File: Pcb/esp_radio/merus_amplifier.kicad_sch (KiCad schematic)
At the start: 2 parts, among them J5 MERUS I2S, J6 MERUS I2C

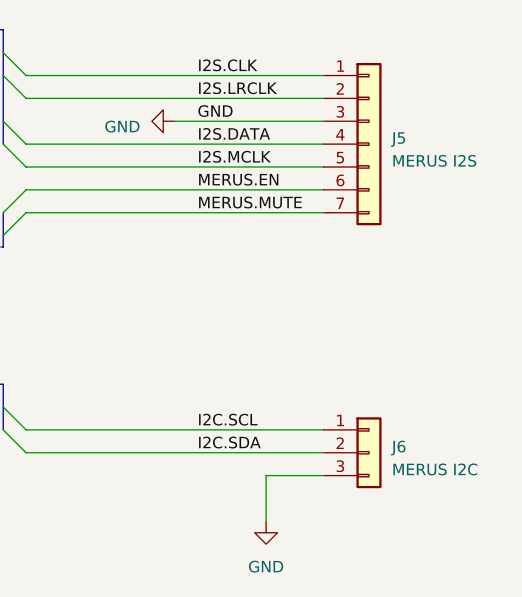
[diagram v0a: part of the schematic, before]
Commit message: Move custom components to kicad_common_library.
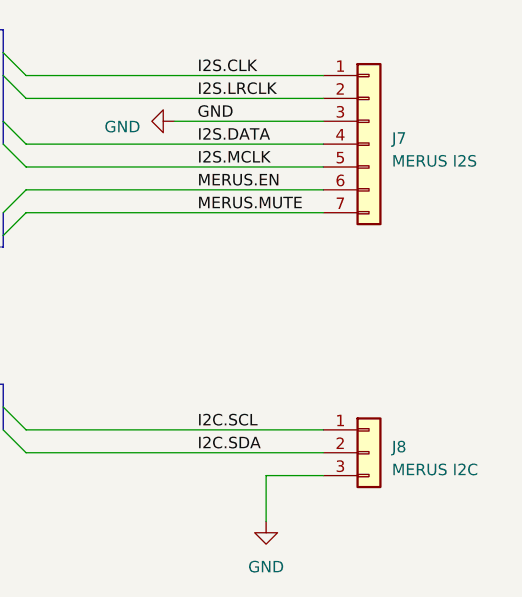
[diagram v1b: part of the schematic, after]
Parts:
- renumbered J5 to J7, J6 to J8
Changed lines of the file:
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@@
   (symbol (lib_id "Connector_Generic:Conn_01x07") (at 170.18 80.01 0) (unit 1)
     (in_bom yes) (on_board yes) (dnp no) (fields_autoplaced)
-    (property "Reference" "J5" (at 172.72 79.375 0)
+    (property "Reference" "J7" (at 172.72 79.375 0)
       (effects (font (size 1.27 1.27)) (justify left))
     )
@@
       (project "esp_radio"
         (path "/c9e2e0d2-0655-4f5e-8e13-71b41b1f7cfe/0a87a903-62c1-40b5-b380-98c846d36513"
-          (reference "J5") (unit 1)
+          (reference "J7") (unit 1)
         )
       )
@@
   (symbol (lib_id "power:GND") (at 158.75 121.92 0) (unit 1)
     (in_bom yes) (on_board yes) (dnp no) (fields_autoplaced)
-    (property "Reference" "#PWR047" (at 158.75 128.27 0)
+    (property "Reference" "#PWR058" (at 158.75 128.27 0)
       (effects (font (size 1.27 1.27)) hide)
     )
@@
       (project "esp_radio"
         (path "/c9e2e0d2-0655-4f5e-8e13-71b41b1f7cfe/0a87a903-62c1-40b5-b380-98c846d36513"
-          (reference "#PWR047") (unit 1)
+          (reference "#PWR058") (unit 1)
         )
       )
@@
   (symbol (lib_id "power:GND") (at 148.59 77.47 270) (unit 1)
     (in_bom yes) (on_board yes) (dnp no) (fields_autoplaced)
-    (property "Reference" "#PWR046" (at 142.24 77.47 0)
+    (property "Reference" "#PWR057" (at 142.24 77.47 0)
       (effects (font (size 1.27 1.27)) hide)
     )
@@
       (project "esp_radio"
         (path "/c9e2e0d2-0655-4f5e-8e13-71b41b1f7cfe/0a87a903-62c1-40b5-b380-98c846d36513"
-          (reference "#PWR046") (unit 1)
+          (reference "#PWR057") (unit 1)
         )
       )
@@
   (symbol (lib_id "Connector_Generic:Conn_01x03") (at 170.18 114.3 0) (unit 1)
     (in_bom yes) (on_board yes) (dnp no) (fields_autoplaced)
-    (property "Reference" "J6" (at 172.72 113.665 0)
+    (property "Reference" "J8" (at 172.72 113.665 0)
       (effects (font (size 1.27 1.27)) (justify left))
     )
@@
       (project "esp_radio"
         (path "/c9e2e0d2-0655-4f5e-8e13-71b41b1f7cfe/0a87a903-62c1-40b5-b380-98c846d36513"
-          (reference "J6") (unit 1)
+          (reference "J8") (unit 1)
         )
       )

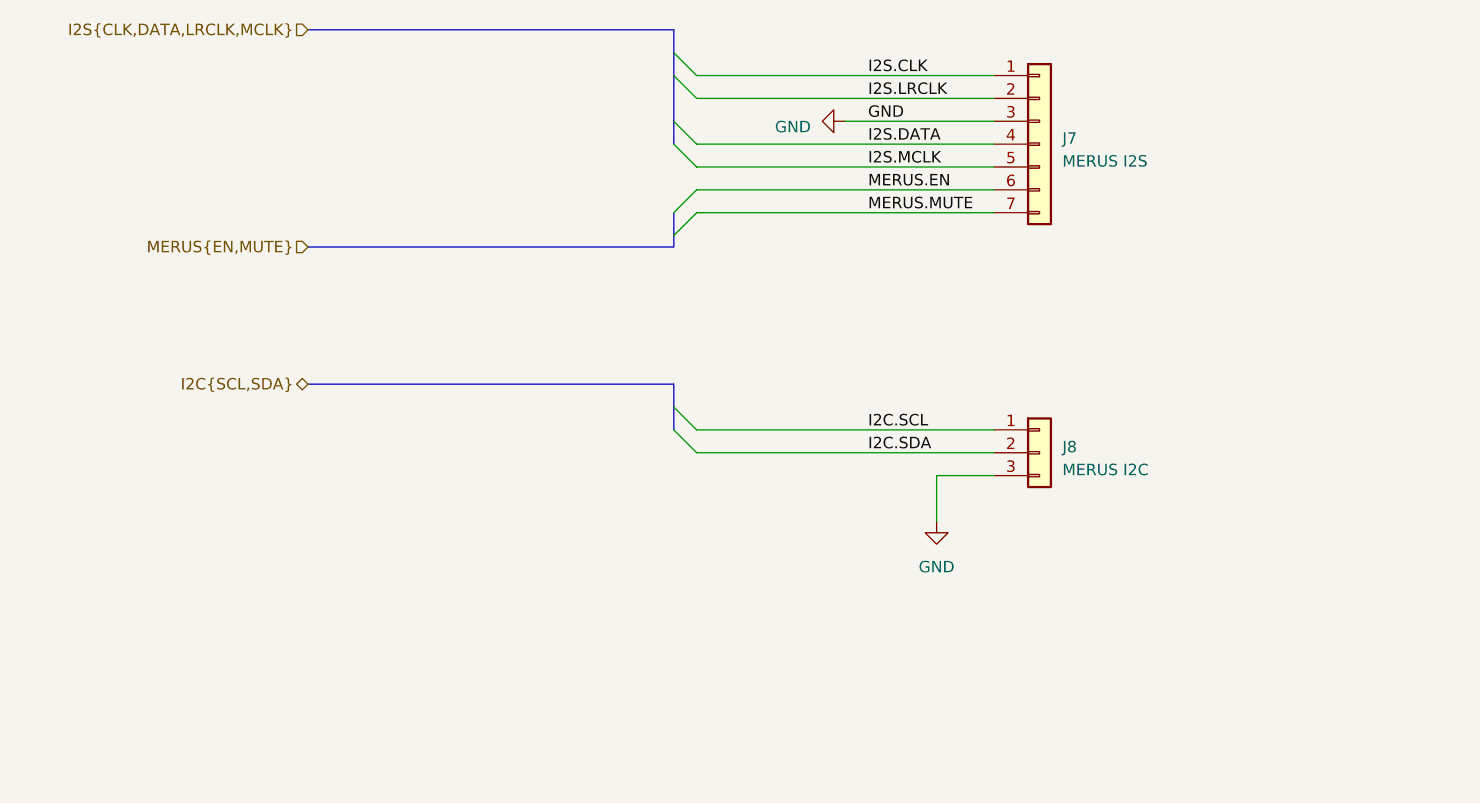
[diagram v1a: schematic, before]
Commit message: Add components layout on PCB
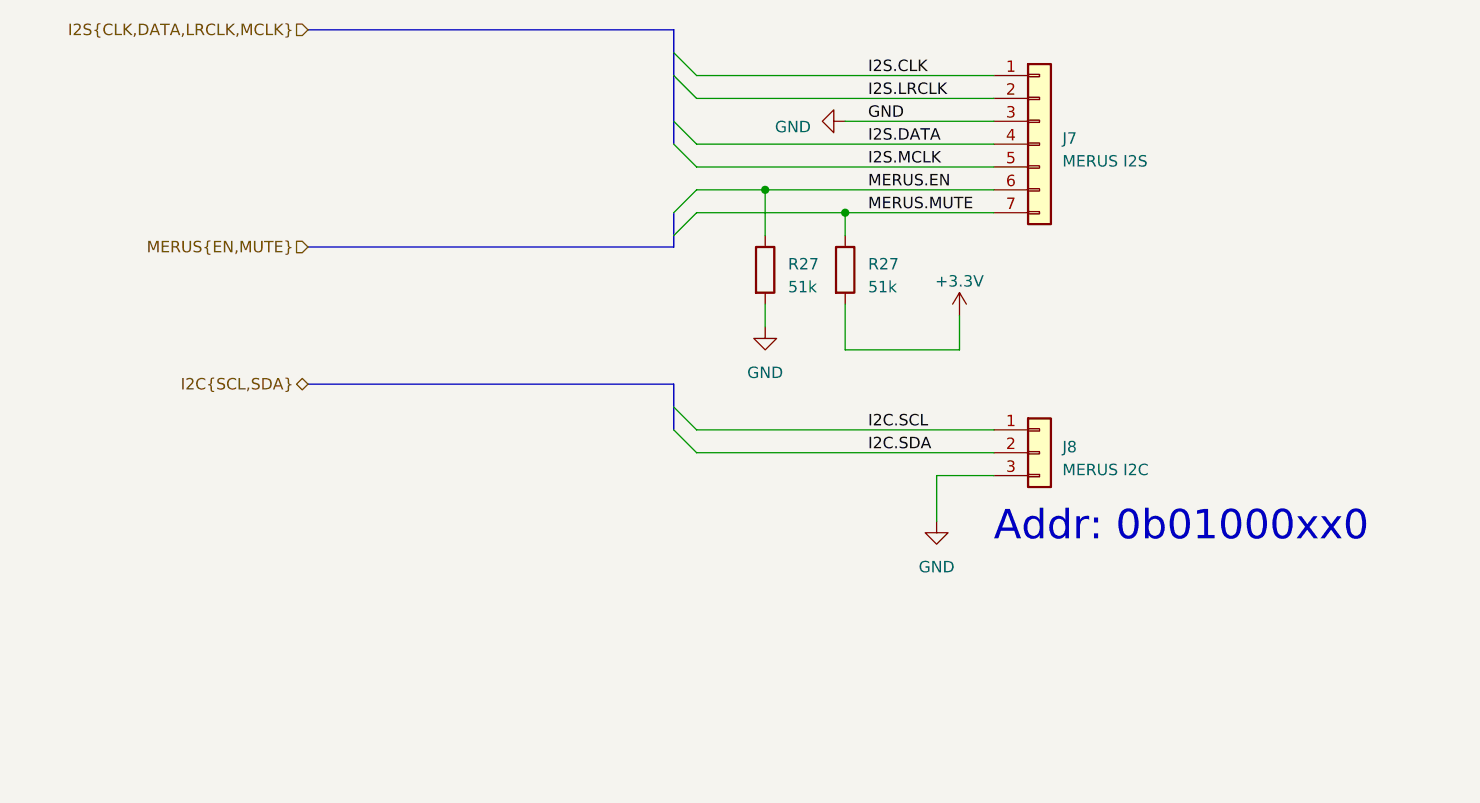
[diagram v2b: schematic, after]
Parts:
- added R27 (x2): 51k, kicad_common_lib:R_0805, symbol Device:R
- J7: footprint (none) -> Connector_JST:JST_XH_S7B-XH-A_1x07_P2.50mm_Horizontal
- J8: footprint (none) -> Connector_JST:JST_XH_S3B-XH-A_1x03_P2.50mm_Horizontal
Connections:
- net GND: now also R27.2
- net MERUS.EN: now also R27.1
- net MERUS.MUTE: now also R27.1
- new net +3.3V: R27.2
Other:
- note added: "Addr: 0b01000xx0"
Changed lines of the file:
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@@
 (kicad_sch (version 20230121) (generator eeschema)
   (paper "A4")
+  (junction (at 148.59 87.63) (diameter 0) (color 0 0 0 0)
+  )
+  (junction (at 139.7 85.09) (diameter 0) (color 0 0 0 0)
+  )
   (bus_entry (at 129.54 69.85) (size 2.54 2.54)
     (stroke (width 0) (type default))
@@
     (stroke (width 0) (type default))
   )
+  (wire (pts (xy 148.59 87.63) (xy 148.59 90.17))
+    (stroke (width 0) (type default))
+  )
   (bus (pts (xy 129.54 67.31) (xy 129.54 69.85))
     (stroke (width 0) (type default))
@@
     (stroke (width 0) (type default))
   )
+  (wire (pts (xy 148.59 102.87) (xy 161.29 102.87))
+    (stroke (width 0) (type default))
+  )
+  (wire (pts (xy 161.29 102.87) (xy 161.29 99.06))
+    (stroke (width 0) (type default))
+  )
   (bus (pts (xy 88.9 106.68) (xy 129.54 106.68))
     (stroke (width 0) (type default))
@@
     (stroke (width 0) (type default))
   )
+  (wire (pts (xy 148.59 87.63) (xy 165.1 87.63))
+    (stroke (width 0) (type default))
+  )
   (bus (pts (xy 129.54 106.68) (xy 129.54 109.22))
     (stroke (width 0) (type default))
@@
     (stroke (width 0) (type default))
   )
-  (wire (pts (xy 132.08 87.63) (xy 165.1 87.63))
+  (wire (pts (xy 139.7 97.79) (xy 139.7 100.33))
+    (stroke (width 0) (type default))
+  )
+  (wire (pts (xy 132.08 87.63) (xy 148.59 87.63))
     (stroke (width 0) (type default))
   )
@@
     (stroke (width 0) (type default))
   )
+  (wire (pts (xy 139.7 85.09) (xy 139.7 90.17))
+    (stroke (width 0) (type default))
+  )
   (wire (pts (xy 132.08 80.01) (xy 165.1 80.01))
     (stroke (width 0) (type default))
   )
-  (wire (pts (xy 132.08 85.09) (xy 165.1 85.09))
+  (wire (pts (xy 132.08 85.09) (xy 139.7 85.09))
     (stroke (width 0) (type default))
   )
@@
     (stroke (width 0) (type default))
   )
+  (wire (pts (xy 139.7 85.09) (xy 165.1 85.09))
+    (stroke (width 0) (type default))
+  )
   (wire (pts (xy 158.75 116.84) (xy 158.75 121.92))
     (stroke (width 0) (type default))
@@
     (stroke (width 0) (type default))
   )
+  (wire (pts (xy 148.59 97.79) (xy 148.59 102.87))
+    (stroke (width 0) (type default))
+  )
   (bus (pts (xy 129.54 77.47) (xy 129.54 80.01))
     (stroke (width 0) (type default))
+  )
+  (text "Addr: 0b01000xx0" (at 165.1 124.46 0)
+    (effects (font (size 3.27 3.27)) (justify left bottom))
   )
   (label "MERUS.EN" (at 151.13 85.09 0) (fields_autoplaced)
@@
     (effects (font (size 1.27 1.27)) (justify right))
   )
+  (symbol (lib_id "power:GND") (at 139.7 100.33 0) (unit 1)
+    (in_bom yes) (on_board yes) (dnp no) (fields_autoplaced)
+    (property "Reference" "#PWR070" (at 139.7 106.68 0)
+      (effects (font (size 1.27 1.27)) hide)
+    )
+    (property "Value" "GND" (at 139.7 105.41 0)
+      (effects (font (size 1.27 1.27)))
+    )
+    (property "Footprint" "" (at 139.7 100.33 0)
+      (effects (font (size 1.27 1.27)) hide)
+    )
+    (property "Datasheet" "" (at 139.7 100.33 0)
+      (effects (font (size 1.27 1.27)) hide)
+    )
+    (pin "1")
+    (instances
+      (project "esp_radio"
+        (path "/c9e2e0d2-0655-4f5e-8e13-71b41b1f7cfe/0a87a903-62c1-40b5-b380-98c846d36513"
+          (reference "#PWR070") (unit 1)
+        )
+      )
+    )
+  )
+  (symbol (lib_id "Device:R") (at 139.7 93.98 0) (unit 1)
+    (in_bom yes) (on_board yes) (dnp no) (fields_autoplaced)
+    (property "Reference" "R27" (at 142.24 93.345 0)
+      (effects (font (size 1.27 1.27)) (justify left))
+    )
+    (property "Value" "51k" (at 142.24 95.885 0)
+      (effects (font (size 1.27 1.27)) (justify left))
+    )
+    (property "Footprint" "kicad_common_lib:R_0805" (at 137.922 93.98 90)
+      (effects (font (size 1.27 1.27)) hide)
+    )
+    (property "Datasheet" "~" (at 139.7 93.98 0)
+      (effects (font (size 1.27 1.27)) hide)
+    )
+    (pin "1")
+    (pin "2")
+    (instances
+      (project "esp_radio"
+        (path "/c9e2e0d2-0655-4f5e-8e13-71b41b1f7cfe/9a87a4f6-9f89-4802-b675-78042b654f8a"
+          (reference "R27") (unit 1)
+        )
+        (path "/c9e2e0d2-0655-4f5e-8e13-71b41b1f7cfe/0a87a903-62c1-40b5-b380-98c846d36513"
+          (reference "R34") (unit 1)
+        )
+      )
+    )
+  )
   (symbol (lib_id "Connector_Generic:Conn_01x07") (at 170.18 80.01 0) (unit 1)
     (in_bom yes) (on_board yes) (dnp no) (fields_autoplaced)
@@
       (effects (font (size 1.27 1.27)) (justify left))
     )
-    (property "Footprint" "" (at 170.18 80.01 0)
+    (property "Footprint" "Connector_JST:JST_XH_S7B-XH-A_1x07_P2.50mm_Horizontal" (at 170.18 80.01 0)
       (effects (font (size 1.27 1.27)) hide)
     )
@@
       (effects (font (size 1.27 1.27)) (justify left))
     )
-    (property "Footprint" "" (at 170.18 114.3 0)
+    (property "Footprint" "Connector_JST:JST_XH_S3B-XH-A_1x03_P2.50mm_Horizontal" (at 170.18 114.3 0)
       (effects (font (size 1.27 1.27)) hide)
     )
@@
         )
       )
+    )
+  )
+  (symbol (lib_id "power:+3.3V") (at 161.29 99.06 0) (unit 1)
+    (in_bom yes) (on_board yes) (dnp no) (fields_autoplaced)
+    (property "Reference" "#PWR037" (at 161.29 102.87 0)
+      (effects (font (size 1.27 1.27)) hide)
+    )
+    (property "Value" "+3.3V" (at 161.29 95.25 0)
+      (effects (font (size 1.27 1.27)))
+    )
+    (property "Footprint" "" (at 161.29 99.06 0)
+      (effects (font (size 1.27 1.27)) hide)
+    )
+    (property "Datasheet" "" (at 161.29 99.06 0)
+      (effects (font (size 1.27 1.27)) hide)
+    )
+    (pin "1")
+    (instances
+      (project "esp_radio"
+        (path "/c9e2e0d2-0655-4f5e-8e13-71b41b1f7cfe/9103cc11-86bf-4fa8-956b-660d9ba42360"
+          (reference "#PWR037") (unit 1)
+        )
+        (path "/c9e2e0d2-0655-4f5e-8e13-71b41b1f7cfe/1eda39b5-ab41-45b2-909c-0f333608d3ad"
+          (reference "#PWR049") (unit 1)
+        )
+        (path "/c9e2e0d2-0655-4f5e-8e13-71b41b1f7cfe/0a87a903-62c1-40b5-b380-98c846d36513"
+          (reference "#PWR071") (unit 1)
+        )
+      )
+    )
+  )
+  (symbol (lib_id "Device:R") (at 148.59 93.98 0) (unit 1)
+    (in_bom yes) (on_board yes) (dnp no) (fields_autoplaced)
+    (property "Reference" "R27" (at 151.13 93.345 0)
+      (effects (font (size 1.27 1.27)) (justify left))
+    )
+    (property "Value" "51k" (at 151.13 95.885 0)
+      (effects (font (size 1.27 1.27)) (justify left))
+    )
+    (property "Footprint" "kicad_common_lib:R_0805" (at 146.812 93.98 90)
+      (effects (font (size 1.27 1.27)) hide)
+    )
+    (property "Datasheet" "~" (at 148.59 93.98 0)
+      (effects (font (size 1.27 1.27)) hide)
+    )
+    (pin "1")
+    (pin "2")
+    (instances
+      (project "esp_radio"
+        (path "/c9e2e0d2-0655-4f5e-8e13-71b41b1f7cfe/9a87a4f6-9f89-4802-b675-78042b654f8a"
+          (reference "R27") (unit 1)
+        )
+        (path "/c9e2e0d2-0655-4f5e-8e13-71b41b1f7cfe/0a87a903-62c1-40b5-b380-98c846d36513"
+          (reference "R35") (unit 1)
+        )
+      )

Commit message: Add chip select emulation for i2c devices
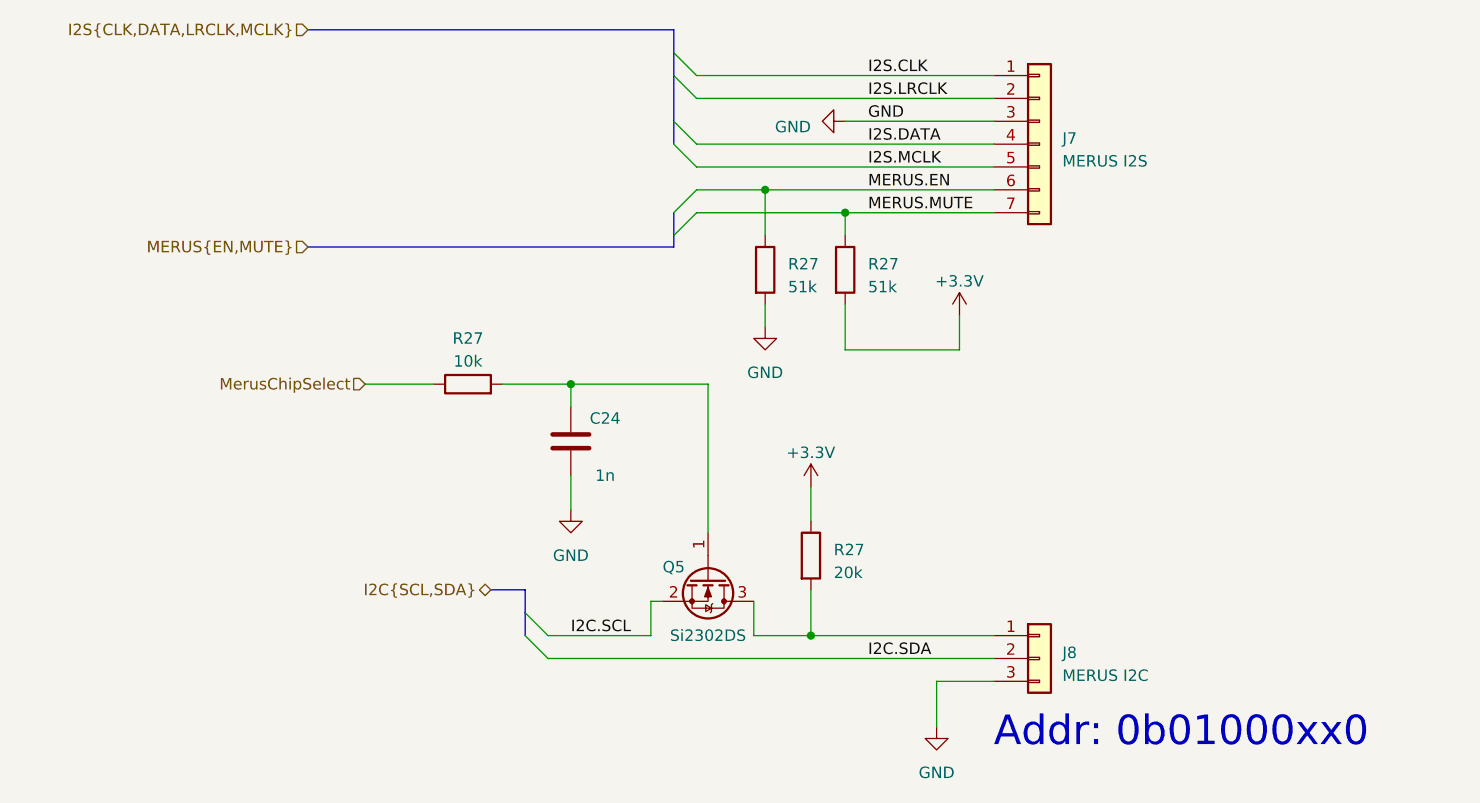
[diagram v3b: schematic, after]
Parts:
- added C24: 1n, kicad_common_lib:C_0805, symbol Device:C
- added Q5: Si2302DS, Package_TO_SOT_SMD:SOT-23, symbol kicad_common_lib:AO3416
- added R27: 10k, kicad_common_lib:R_0805, symbol Device:R
- added R27: 20k, kicad_common_lib:R_0805, symbol Device:R
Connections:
- net +3.3V: now also R27.1
- net GND: now also C24.2
- net I2C.SCL: now also Q5.2 (S); no longer J8.1 (Pin_1)
- new net: C24.1, Q5.1 (G), R27.2
- new net: J8.1 (Pin_1), Q5.3 (D), R27.2
- new net MerusChipSelect: R27.1
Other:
- moved on the sheet: J8

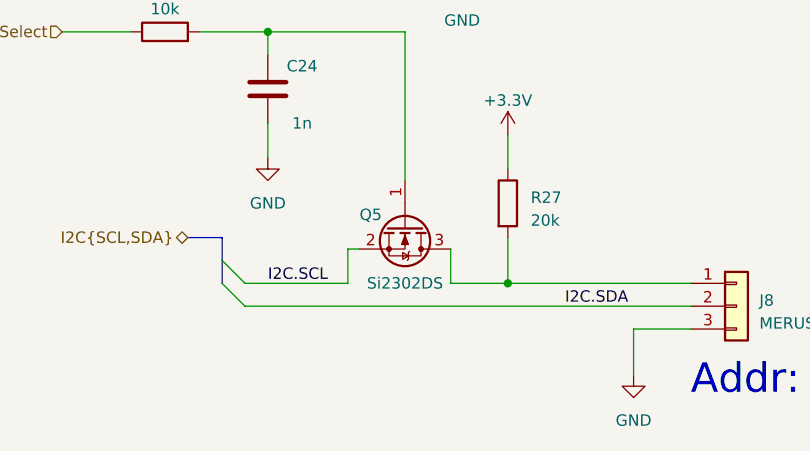
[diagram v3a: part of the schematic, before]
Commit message: Export gerber file.
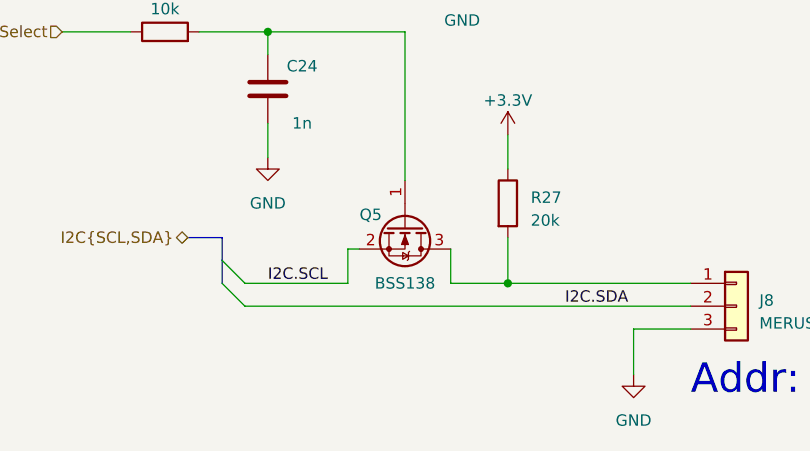
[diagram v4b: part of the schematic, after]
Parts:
- Q5: value Si2302DS -> BSS138
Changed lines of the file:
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@@
       (effects (font (size 1.27 1.27)))
     )
-    (property "Value" "Si2302DS" (at 133.35 134.62 90)
+    (property "Value" "BSS138" (at 133.35 134.62 90)
       (effects (font (size 1.27 1.27)))
     )
